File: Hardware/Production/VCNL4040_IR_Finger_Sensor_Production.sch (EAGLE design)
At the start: 11 parts, among them U1 VCNL4040

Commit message: Adding examples. Testing JST on milled layout.
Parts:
- added U$3, U$4: STAND-OFF, SparkX:STAND-OFF
- J1: device SparkFun-Connectors:CONN_05 -> SparkFun-Connectors:CONN_04SMD2
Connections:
- net 3.3V: now also J1.2; no longer J1.4
- net GND: now also J1.1; no longer J1.5
- net INT: no longer J1.1
- net SCL: now also J1.4; no longer J1.2
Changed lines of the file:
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@@
 <?xml version="1.0" encoding="utf-8"?>
 <!DOCTYPE eagle SYSTEM "eagle.dtd">
-<eagle version="7.6.0">
+<eagle version="7.7.0">
 <drawing>
 <settings>
@@
 <part name="U$2" library="SparkX" deviceset="SPARKX-LOGO" device="2"/>
 <part name="U1" library="SparkX" deviceset="VCNL4040" device=""/>
-<part name="J1" library="SparkFun-Connectors" deviceset="CONN_05" device=""/>
 <part name="R3" library="SparkFun-Resistors" deviceset="8.2KOHM" device="-0603-1/10W-5%" value="8.2k"/>
 <part name="SUPPLY4" library="SparkFun-PowerSymbols" deviceset="3.3V" device=""/>
+<part name="J1" library="SparkFun-Connectors" deviceset="CONN_04" device="SMD2"/>
+<part name="U$3" library="SparkX" deviceset="STAND-OFF" device=""/>
+<part name="U$4" library="SparkX" deviceset="STAND-OFF" device=""/>
 </parts>
 <sheets>
@@
 <instance part="U$2" gate="G$1" x="182.88" y="48.26"/>
 <instance part="U1" gate="G$1" x="114.3" y="109.22"/>
-<instance part="J1" gate="G$1" x="76.2" y="27.94" rot="R180"/>
 <instance part="R3" gate="G$1" x="139.7" y="132.08" rot="R90"/>
 <instance part="SUPPLY4" gate="G$1" x="139.7" y="139.7"/>
+<instance part="J1" gate="G$1" x="73.66" y="25.4" rot="MR0"/>
+<instance part="U$3" gate="G$1" x="238.76" y="30.48"/>
+<instance part="U$4" gate="G$1" x="236.22" y="30.48"/>
 </instances>
 <busses>
@@
 <pinref part="GND4" gate="1" pin="GND"/>
 <wire x1="55.88" y1="20.32" x2="55.88" y2="22.86" width="0.1524" layer="91"/>
-<pinref part="J1" gate="G$1" pin="5"/>
+<pinref part="J1" gate="G$1" pin="1"/>
 </segment>
 </net>
@@
 <wire x1="68.58" y1="30.48" x2="66.04" y2="30.48" width="0.1524" layer="91"/>
 <label x="66.04" y="30.48" size="1.27" layer="95" rot="MR0" xref="yes"/>
-<pinref part="J1" gate="G$1" pin="2"/>
+<pinref part="J1" gate="G$1" pin="4"/>
 </segment>
 <segment>
@@
 <junction x="139.7" y="106.68"/>
 </segment>
-<segment>
-<wire x1="68.58" y1="33.02" x2="66.04" y2="33.02" width="0.1524" layer="91"/>
-<label x="66.04" y="33.02" size="1.27" layer="95" rot="R180" xref="yes"/>
-<pinref part="J1" gate="G$1" pin="1"/>
-</segment>
 </net>
 <net name="3.3V" class="0">
@@
 <wire x1="55.88" y1="40.64" x2="55.88" y2="25.4" width="0.1524" layer="91"/>
 <pinref part="SUPPLY8" gate="G$1" pin="3.3V"/>
-<pinref part="J1" gate="G$1" pin="4"/>
-</segment>
-<segment>
+<pinref part="J1" gate="G$1" pin="2"/>
+</segment>
+<segment>

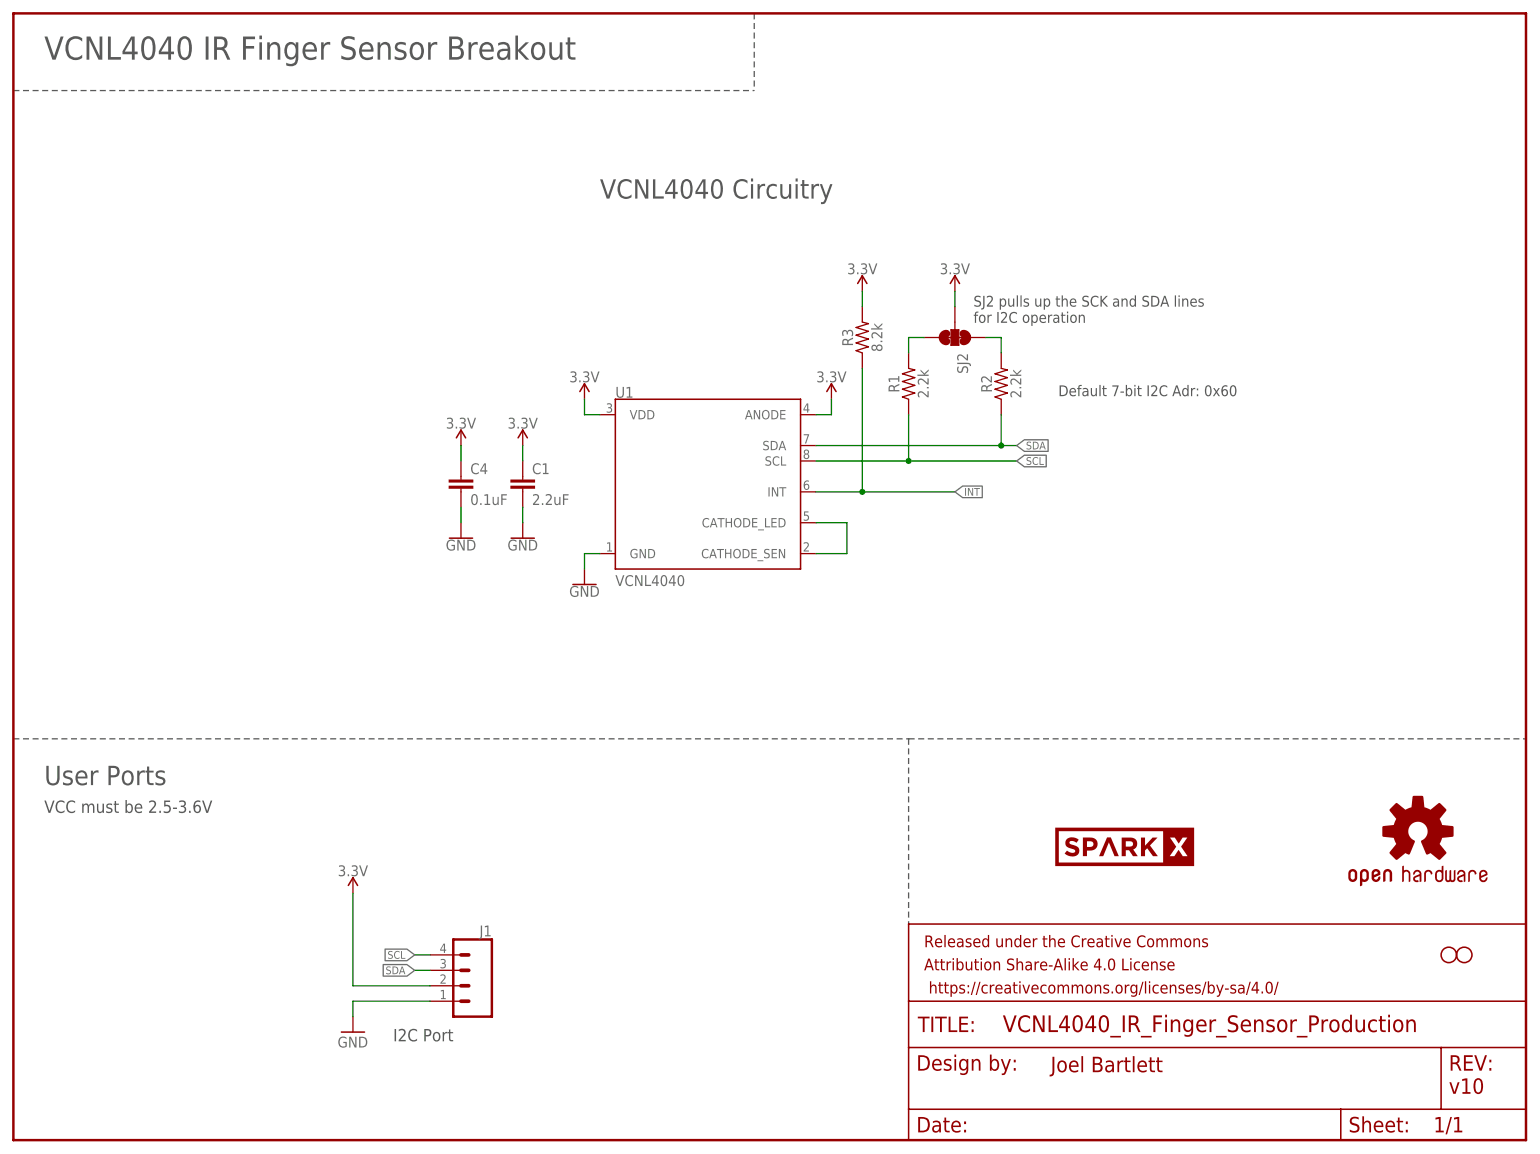
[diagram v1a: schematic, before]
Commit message: Adding production panel
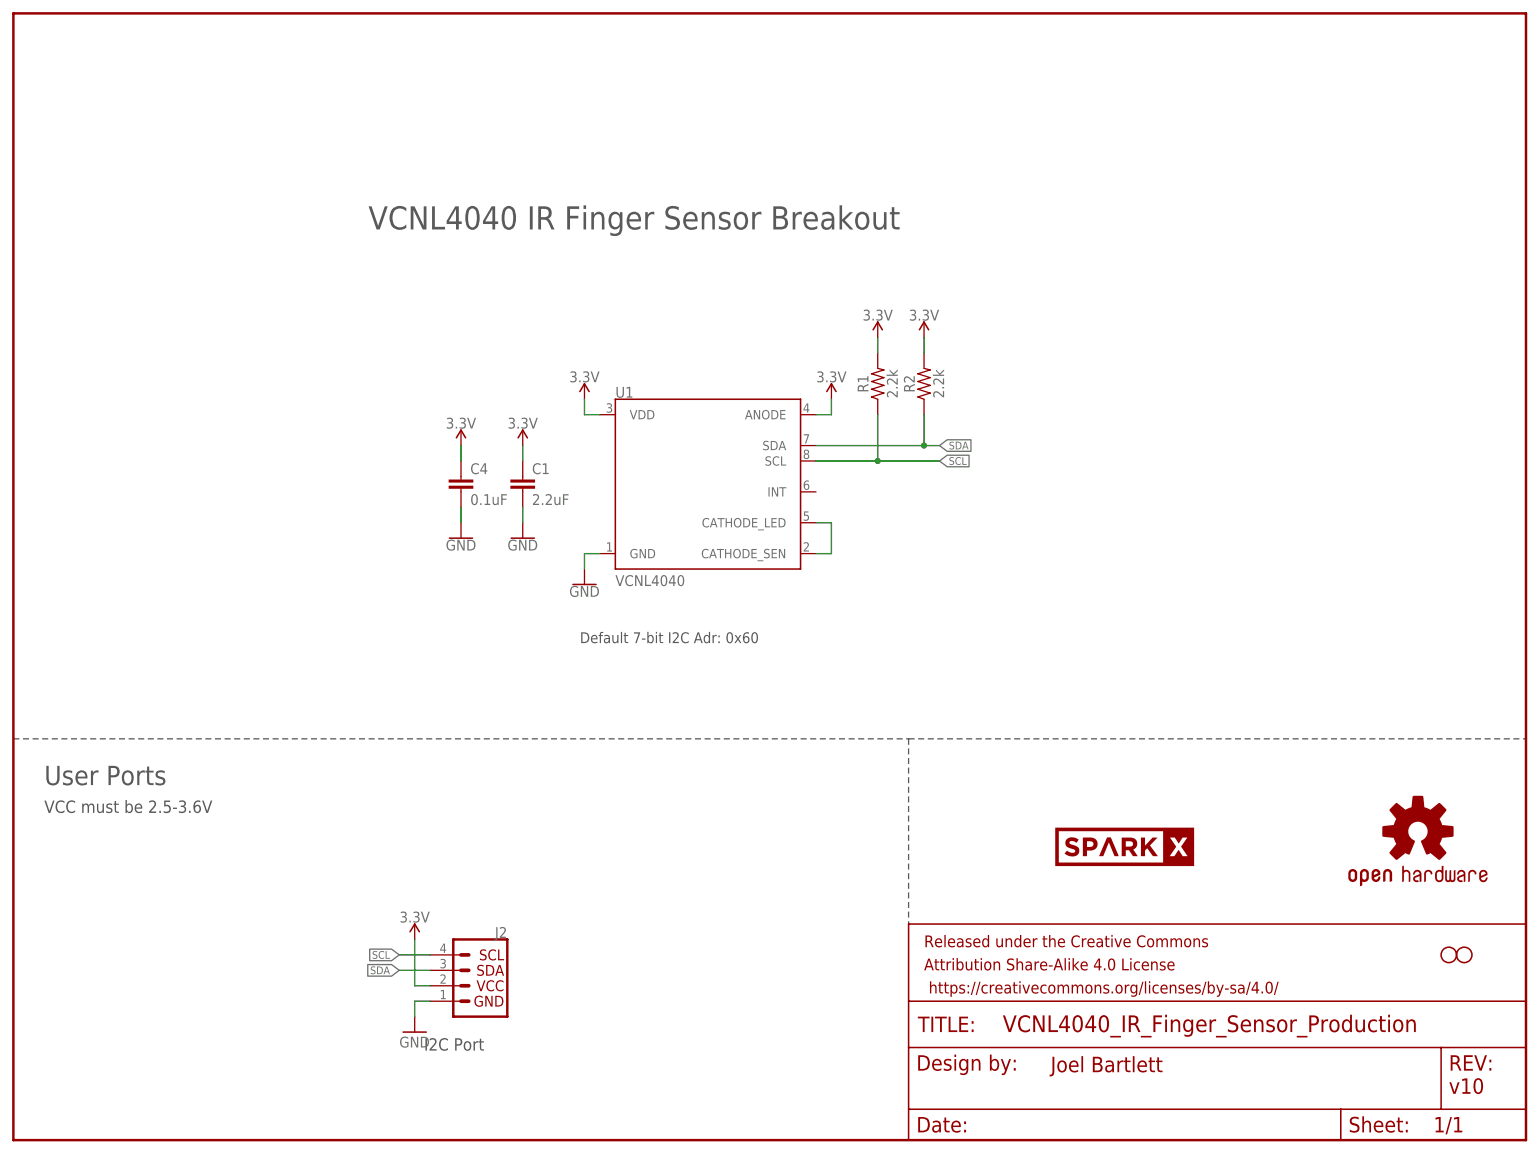
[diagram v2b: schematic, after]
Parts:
- removed J1: (no value), SparkFun-Connectors:CONN_04SMD2
- removed R3: 8.2k, SparkFun-Resistors:8.2KOHM-0603-1/10W-5%
- removed SJ2: (no value), TestAperatures:JUMPER-PAD-3-NC_BY_TRACE
- added J2: (no value), SparkX:I2C_STANDARDJS-1MM
- U$2: value SPARKX-LOGO2 -> SPARKX-LOGO3; device SparkX:SPARKX-LOGO2 -> SparkX:SPARKX-LOGO3
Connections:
- removed net INT: R3.1, U1.INT
- removed net N$4: R2.2, SJ2.1
- removed net N$5: R1.2, SJ2.3
- net 3.3V: now also J2.VCC, R1.2, R2.2; no longer J1.2, R3.2, SJ2.2
- net GND: now also J2.GND; no longer J1.1
- net SCL: now also J2.SCL; no longer J1.4
- net SDA: now also J2.SDA; no longer J1.3
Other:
- note removed: "SJ2 pulls up the SCK and SDA lines for I2C operation"
- note removed: "VCNL4040 Circuitry"
- moved on the sheet: R1, R2
